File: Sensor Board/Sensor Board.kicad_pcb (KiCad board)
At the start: 2 copper layers, 44 parts, among them J1 Programming Header, J3 Micro_SD_Card, J4 CAN Bus Connector, U1 PIC18F26K83, U2 SPX3819M5-L-3-3, U3 MCP2562, U4 INA180, U5 OPA323IDCKR, Y1 12MHz Crystal

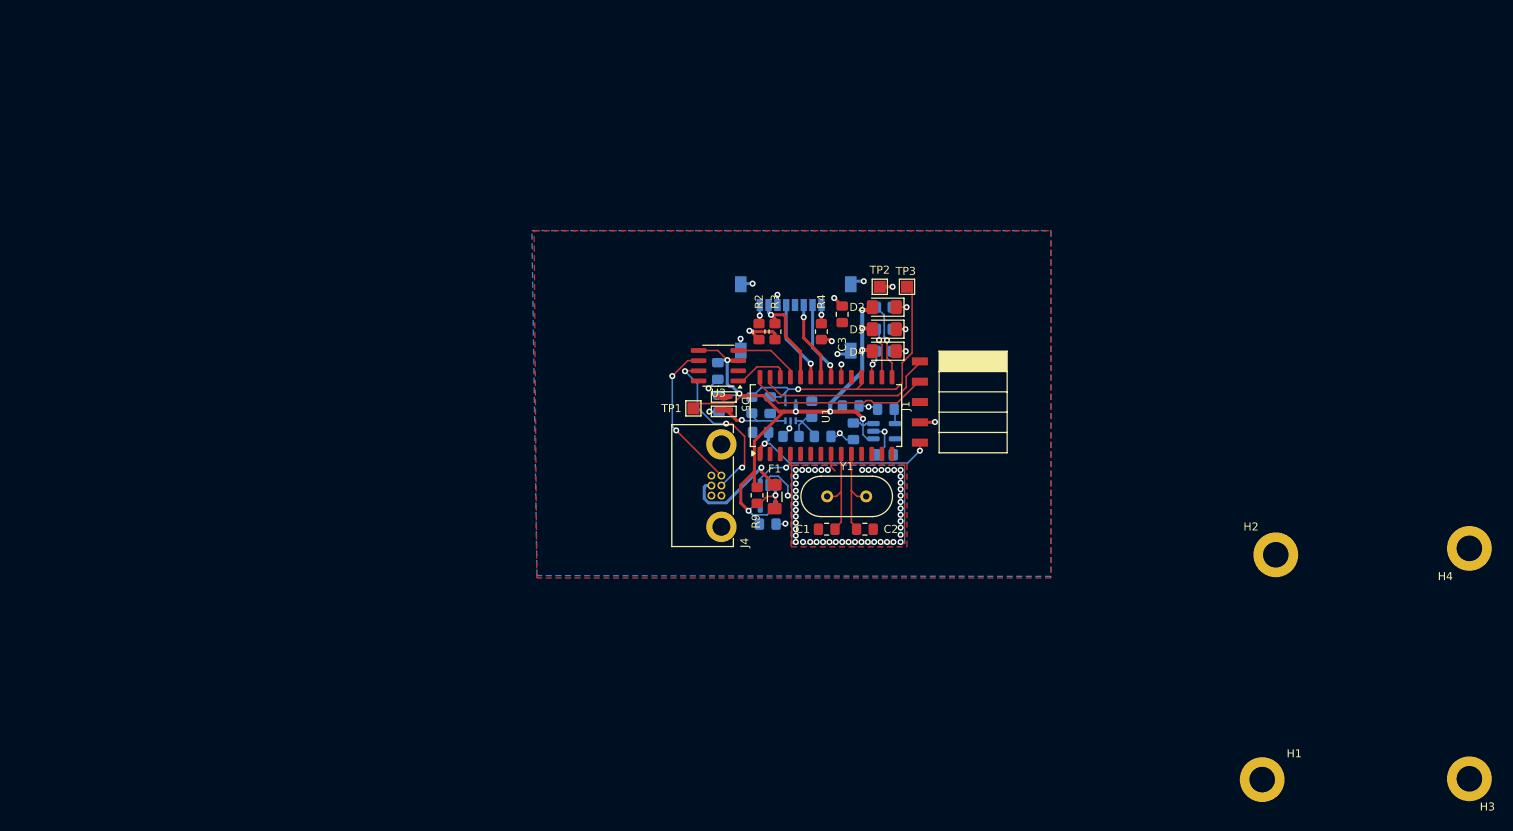
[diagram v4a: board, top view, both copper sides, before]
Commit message: fixed footprints not loading
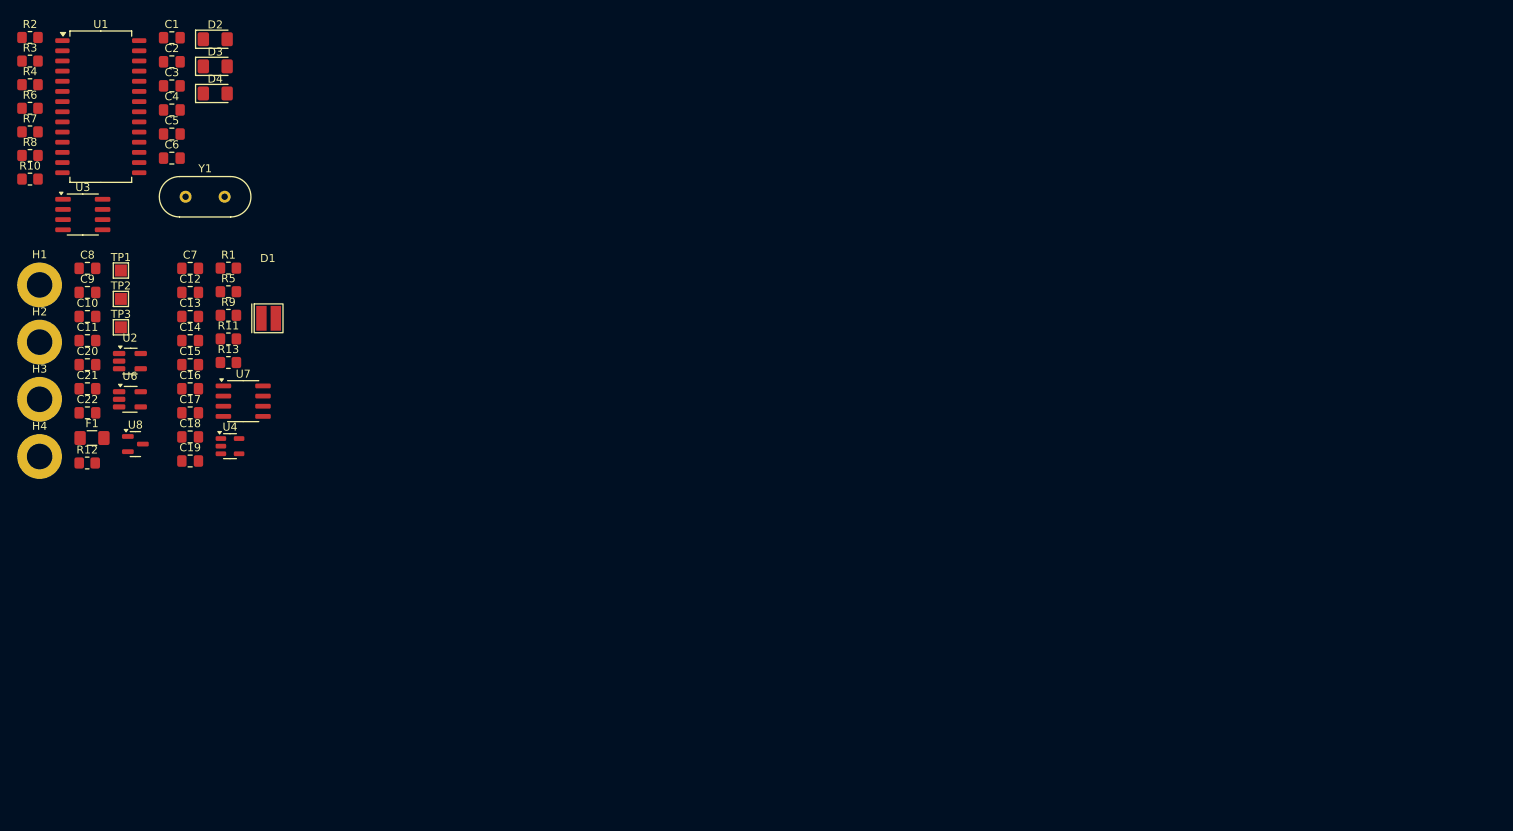
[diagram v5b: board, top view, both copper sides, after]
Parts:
- removed D5: Irr Sense, Canhw:P16612-011CA
- removed J1: Programming Header, Canhw:PinSocket_5x2.54_SMD_90deg_952-3198-1-ND
- removed J3: Micro_SD_Card, Canhw:microSD_Molex_WM6698CT-ND
- removed J4: CAN Bus Connector, Canhw:connector_Harwin_G125–MG10605M4P
- removed U5: OPA323IDCKR, Canhw:SC70-5_DCK_TEX
- added C14: 0.1uF, Capacitor_SMD:C_0805_2012Metric_Pad1.18x1.45mm_HandSolder, F.Cu at (70.7, 75.7)
- added C15: 0.1uF, Capacitor_SMD:C_0805_2012Metric_Pad1.18x1.45mm_HandSolder, F.Cu at (70.7, 78.7)
- added C16: 0.1uF, Capacitor_SMD:C_0805_2012Metric_Pad1.18x1.45mm_HandSolder, F.Cu at (70.7, 81.7)
- added C17: 0.1uF, Capacitor_SMD:C_0805_2012Metric_Pad1.18x1.45mm_HandSolder, F.Cu at (70.7, 84.8)
- added C18: 2.2uF, Capacitor_SMD:C_0805_2012Metric_Pad1.18x1.45mm_HandSolder, F.Cu at (70.7, 87.8)
- added C19: 2.2uF, Capacitor_SMD:C_0805_2012Metric_Pad1.18x1.45mm_HandSolder, F.Cu at (70.7, 90.8)
- added C20: 0.1uF, Capacitor_SMD:C_0805_2012Metric_Pad1.18x1.45mm_HandSolder, F.Cu at (57.9, 78.7)
- added C21: 1uF, Capacitor_SMD:C_0805_2012Metric_Pad1.18x1.45mm_HandSolder, F.Cu at (57.9, 81.7)
- added C22: 10uF, Capacitor_SMD:C_0805_2012Metric_Pad1.18x1.45mm_HandSolder, F.Cu at (57.9, 84.8)
- added C8: 0.1uF, Capacitor_SMD:C_0805_2012Metric_Pad1.18x1.45mm_HandSolder, F.Cu at (57.9, 66.7)
- added D1: P16612-011CA, SensorBoardFootprints:P16612-011CA, F.Cu at (80.4, 65.9)
- added R12: 200mR, Resistor_SMD:R_0805_2012Metric_Pad1.20x1.40mm_HandSolder, F.Cu at (57.8, 91.0)
- added R13: 10R, Resistor_SMD:R_0805_2012Metric_Pad1.20x1.40mm_HandSolder, F.Cu at (75.5, 78.5)
- added U6: SPX3819M5-L-3-3, Package_TO_SOT_SMD:SOT-23-5_HandSoldering, F.Cu at (63.2, 83.1)
- added U7: MCP1501-25xSN, Package_SO:SOIC-8_3.9x4.9mm_P1.27mm, F.Cu at (77.3, 83.3)
- added U8: MCP1754S-3302xCB, Package_TO_SOT_SMD:SOT-23, F.Cu at (63.8, 88.7)
- C10: value 10nF -> 0.1uF; moved to F.Cu
- C11: value 1uF -> 10nF; moved to F.Cu
- C12: value 2.5pF -> 1uF; moved to F.Cu
- C13: value 1uF -> 0.1uF; moved to F.Cu
- C4, C5, C6, C9, R10, R6, R7, R8: moved to F.Cu
- C7: value 0.1uF -> 4.7pF; moved to F.Cu
- R1: value 3MR -> 3.2M; moved to F.Cu
- R11: value 1kR -> 10R; moved to F.Cu
- R5: value 31kR -> 9.31k; moved to F.Cu
- R9: value 200mR -> 287R
- TP2: value 3.3v -> 3V3D
- TP3: value TestPoint -> 3V3A
- U2: value SPX3819M5-L-3-3 -> INA180; moved to F.Cu
- U4: value INA180 -> OPA323; footprint Package_TO_SOT_SMD:SOT-23-5_HandSoldering -> Package_TO_SOT_SMD:SOT-23-5; moved to F.Cu
- moved H3 184.9 mm to (51.9, 83.1)
- moved H4 179.1 mm to (51.9, 90.2)
- moved H1 164.9 mm to (51.9, 68.8)
- moved H2 156.8 mm to (51.9, 75.9)
- moved R6 109.6 mm to (50.7, 46.7), turned to 0 degrees
- moved R7 109.6 mm to (50.7, 49.6), turned to 0 degrees
- moved R10 108.9 mm to (50.7, 55.5), turned to 0 degrees
- moved C2 104.5 mm to (68.4, 40.9)
- moved R4 103.6 mm to (50.7, 43.7), turned to 0 degrees
- moved C1 102.3 mm to (68.4, 37.9), turned to 0 degrees
- moved C11 100.7 mm to (57.9, 75.7), turned to 0 degrees
- moved C10 100.5 mm to (57.9, 72.7), turned to 0 degrees
- moved R3 99.1 mm to (50.7, 40.8), turned to 0 degrees
- moved U1 98.5 mm to (59.5, 46.5), turned to 0 degrees
- moved TP3 98.4 mm to (62.0, 74.1)
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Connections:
- C10 pad 1: Net-(U2-BP) -> +5V
- C10 pad 2: GND -> AGND
- C11 pad 1: +3.3V -> Net-(U6-BP)
- C12 pad 1: /IRR_SENSE -> AGND
- C12 pad 2: Net-(D5-A) -> Net-(U4-+)
- C13 pad 1: GND -> AGND
- C13 pad 2: Net-(U5-IN+) -> Net-(U5-AVDD)
- C3 pad 2: +3.3V -> +3V3D
- C4 pad 1: +3.3V -> +3V3D
- C5 pad 2: +5V -> +3V3D
- C7 pad 1: +5V -> Net-(D1-A)
- C7 pad 2: GND -> Net-(U5-CH0)
- F1 pad 2: Net-(U4-IN+) -> Net-(U2-IN+)
- R1 pad 1: Net-(D5-A) -> Net-(D1-A)
- R1 pad 2: /IRR_SENSE -> Net-(U5-CH0)
- R11 pad 1: Net-(U5-IN+) -> +3V3A
- R11 pad 2: GND -> Net-(U5-AVDD)
- R2 pad 1: +3.3V -> +3V3D
- R3 pad 1: +3.3V -> +3V3D
- R4 pad 1: +3.3V -> +3V3D
- R5 pad 1: Net-(U5-IN+) -> +3V3A
- R5 pad 2: +3.3V -> Net-(U4-+)
- R6 pad 2: Net-(U1-RC4) -> Net-(U1-RA3)
- R7 pad 2: Net-(U1-RC5) -> Net-(U1-RA4)
- R8 pad 1: +3.3V -> +3V3D
- R9 pad 1: +5V -> AGND
- R9 pad 2: Net-(U4-IN+) -> Net-(U4-+)
- TP2 pad 1: +3.3V -> +3V3D
- TP3 pad 1: /IRR_SENSE -> +3V3A
- U1 pad 14: unconnected-(U1-RC3-Pad14) -> /SCLK
- U1 pad 15: Net-(U1-RC4) -> /MOSI
- U1 pad 16: Net-(U1-RC5) -> /MISO
- U1 pad 2: unconnected-(U1-RA0-Pad2) -> /MCLKIN
- U1 pad 20: +3.3V -> +3V3D
- U1 pad 3: unconnected-(U1-RA1-Pad3) -> /IRQ/MDAT
- U1 pad 5: unconnected-(U1-RA3-Pad5) -> Net-(U1-RA3)
- U1 pad 6: unconnected-(U1-RA4-Pad6) -> Net-(U1-RA4)
- U1 pad 7: unconnected-(U1-RA5-Pad7) -> /CS
- U2 pad 1: +5V -> /CURR_SENSE
- U2 pad 3: +5V -> Net-(U2-IN+)
- U2 pad 4: Net-(U2-BP) -> +5V
- U2 pad 5: +3.3V -> +3V3
- U3 pad 5: +5V -> +3V3D
- U4 pad 1: /CURR_SENSE -> Net-(U5-CH0)
- U4 pad 2: GND -> AGND
- U4 pad 3: Net-(U4-IN+) -> Net-(U4-+)
- U4 pad 4: +5V -> Net-(D1-A)
- U4 pad 5: +5V -> +3V3A
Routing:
- net +5V: track 88.6 -> 0.00 mm, vias 9 -> 0
- net /IRR_SENSE: track 38.1 -> 0.00 mm, vias 1 -> 0
- net GND: track 33.2 -> 0.00 mm, vias 63 -> 0
- net /~{MCLR}: track 25.7 -> 0.00 mm, vias 2 -> 0
- net /ICSPDAT: track 23.2 -> 0.00 mm
- net /ICSPCLK: track 22.9 -> 0.00 mm
- net /CANH: track 21.8 -> 0.00 mm, vias 3 -> 0
- net /CANL: track 19.1 -> 0.00 mm, vias 2 -> 0
- net Net-(J2-Pin_5): track 14.4 -> 0.00 mm, vias 1 -> 0
- net +3.3V: track 13.9 -> 0.00 mm, vias 6 -> 0
- net /PIC_MICRO_SD_SDI: track 12.9 -> 0.00 mm, vias 1 -> 0
- net /OSC2: track 11.8 -> 0.00 mm
- net /OSC1: track 11.7 -> 0.00 mm
- net Net-(D5-A): track 10.8 -> 0.00 mm, vias 1 -> 0
- net /PIC_MICRO_SD_SCK: track 10.3 -> 0.00 mm, vias 1 -> 0
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- removed copper zone on B.Cu, net +3.3V
- removed copper zone on B.Cu, net GND
- removed copper zone on F.Cu, net GND

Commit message: did layout
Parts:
- removed R2: 10kR, Resistor_SMD:R_0805_2012Metric_Pad1.20x1.40mm_HandSolder
- removed TP1: 5v, TestPoint:TestPoint_Pad_1.5x1.5mm
- removed TP2: 3V3D, TestPoint:TestPoint_Pad_1.5x1.5mm
- removed TP3: 3V3A, TestPoint:TestPoint_Pad_1.5x1.5mm
- added +3V3A: 3V3A, TestPoint:TestPoint_Pad_1.5x1.5mm, F.Cu at (221.7, 72.6)
- added +3V3D: 3V3D, TestPoint:TestPoint_Pad_1.5x1.5mm, F.Cu at (221.7, 77.7)
- added +5V: 5v, TestPoint:TestPoint_Pad_1.5x1.5mm, F.Cu at (221.7, 75.2)
- added C23: 0.1uF, Capacitor_SMD:C_0805_2012Metric_Pad1.18x1.45mm_HandSolder, F.Cu at (207.5, 59.7)
- added G***: LOGO, Team_Logo:Logo_SilkScreen_5mm, F.Cu at (191.0, 100.1)
- added J1: Programming Header, canhw:PinSocket_5x2.54_SMD_90deg_952-3198-1-ND, F.Cu at (190.5, 65.9)
- added J2: CAN Bus Connector, canhw:connector_Harwin_G125–MG10605M4P, F.Cu at (220.3, 87.1)
- added J3: Micro_SD_Card, canhw:microSD_Molex_WM6698CT-ND, B.Cu at (208.8, 100.8)
- added R14: 10kR, Resistor_SMD:R_0805_2012Metric_Pad1.20x1.40mm_HandSolder, B.Cu at (191.5, 100.6)
- added U5: MCP3561-E/ST, Package_SO:TSSOP-20_4.4x6.5mm_P0.65mm, F.Cu at (209.4, 71.4)
- C10, C11, C20, C21, C22, C3, C8, C9, F1, R12, R3, U2, U6, U8: moved to B.Cu
- moved R3 173.2 mm to (212.9, 101.6), turned to 180 degrees
- moved H2 169.9 mm to (220.0, 100.3)
- moved H1 168.4 mm to (220.0, 58.7)
- moved C11 161.4 mm to (217.9, 96.0)
- moved R4 160.0 mm to (201.2, 98.0), turned to 180 degrees
- moved U3 159.3 mm to (211.8, 98.6)
- moved C22 158.9 mm to (215.9, 68.6), turned to 180 degrees
- moved C20 158.6 mm to (215.9, 66.0), turned to 180 degrees
- moved F1 158.0 mm to (216.4, 85.6), turned to 90 degrees
- moved C9 155.5 mm to (211.9, 90.9), turned to -90 degrees
- moved R12 155.2 mm to (212.9, 85.1), turned to 90 degrees
- moved C21 155.1 mm to (212.3, 95.5), turned to 180 degrees
- moved C10 154.4 mm to (212.2, 72.1), turned to 90 degrees
- moved C5 154.2 mm to (213.4, 102.6)
- moved C3 153.8 mm to (212.3, 98.0)
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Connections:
- C8 pad 1: +3V3 -> +3V3D
- H1 pad 1: GND -> unconnected-(H1-Pad1)
- R10 pad 2: Net-(U1-RC6) -> Net-(U1-RA2)
- R13 pad 1: +3V3A -> +3V3D
- R3 pad 2: /PIC_MICRO_SD_SDI -> /MISO
- R4 pad 2: Net-(J3-DAT2) -> /MOSI
- U1 pad 11: unconnected-(U1-RC0-Pad11) -> /CANRX
- U1 pad 12: unconnected-(U1-RC1-Pad12) -> /CANTX
- U1 pad 15: /MOSI -> /MISO
- U1 pad 16: /MISO -> /MOSI
- U1 pad 17: Net-(U1-RC6) -> /CS_SD
- U1 pad 18: /IRR_SENSE -> unconnected-(U1-RC7-Pad18)
- U1 pad 21: /PIC_MICRO_SD_CS -> unconnected-(U1-RB0-Pad21)
- U1 pad 22: /PIC_MICRO_SD_SDO -> unconnected-(U1-RB1-Pad22)
- U1 pad 23: /PIC_MICRO_SD_SCK -> unconnected-(U1-RB2-Pad23)
- U1 pad 24: /PIC_MICRO_SD_SDI -> unconnected-(U1-RB3-Pad24)
- U1 pad 25: /CANRX -> unconnected-(U1-RB4-Pad25)
- U1 pad 26: /CANTX -> /CURR_SENSE
- U1 pad 4: /CURR_SENSE -> Net-(U1-RA2)
- U1 pad 7: /CS -> /CS_ADC
- U2 pad 5: +3V3 -> +3V3D
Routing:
- net +5V: track 0.00 -> 68.2 mm, vias 0 -> 6
- net /SCLK: track 0.00 -> 46.6 mm, vias 0 -> 1
- net /MISO: track 0.00 -> 39.2 mm, vias 0 -> 1
- net /~{MCLR}: track 0.00 -> 35.5 mm, vias 0 -> 3
- net /MOSI: track 0.00 -> 35.1 mm, vias 0 -> 1
- net +3V3D: track 0.00 -> 31.1 mm, vias 0 -> 20
- net /CANTX: track 0.00 -> 28.8 mm
- net /ICSPCLK: track 0.00 -> 27.9 mm, vias 0 -> 2
- net /ICSPDAT: track 0.00 -> 27.5 mm, vias 0 -> 2
- net /CANRX: track 0.00 -> 25.6 mm
- net /CS_ADC: track 0.00 -> 21.3 mm
- net GND: track 0.00 -> 21.0 mm, vias 0 -> 44
- net /MCLKIN: track 0.00 -> 20.9 mm
- net /CS_SD: track 0.00 -> 20.7 mm, vias 0 -> 1
- net /CANL: track 0.00 -> 20.6 mm
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- added copper zone on B.Cu, net +3V3A
- added copper zone on In2.Cu, net +3V3A
- added copper zone on B.Cu, net +3V3D
- added copper zone on In2.Cu, net +3V3D
- added copper zone on B.Cu, net +5V
- added copper zone on B.Cu, net AGND
- added copper zone on F.Cu, net AGND
- added copper zone on In1.Cu, net AGND
- added copper zone on B.Cu, net GND
- added copper zone on F.Cu, net GND
- added copper zone on In1.Cu, net GND
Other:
- board outline added: 41.7 x 49.5 mm
- copper layers 2 -> 4
- board text added: "1mW Infrared Detector DO NOT TOUCH LENSE KEEP OUT OF SUN 350mA @ 5V"
- board text added: "HOT!"
- board text added: "IR-Relevant Connor Stubbs Manav Toor 24-05-2025"
- board text added: "Waterloo Rocketry"
- board text added: "~{MCLR}"

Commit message: connected grounds
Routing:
- net (no net): track 0.00 -> 2.03 mm
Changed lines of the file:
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@@
 			(size 3.8 3.8)
 			(drill 2.25)
-			(layers "*.Cu" "*.Mask")
+			(layers "*.Cu" "*.Mask" "In3.Cu" "In4.Cu" "In5.Cu" "In6.Cu" "In7.Cu" "In8.Cu"
+				"In9.Cu" "In10.Cu" "In11.Cu" "In12.Cu" "In13.Cu" "In14.Cu" "In15.Cu"
+				"In16.Cu" "In17.Cu" "In18.Cu" "In19.Cu" "In20.Cu" "In21.Cu" "In22.Cu"
+				"In23.Cu" "In24.Cu" "In25.Cu" "In26.Cu" "In27.Cu" "In28.Cu" "In29.Cu"
+				"In30.Cu"
+			)
 			(remove_unused_layers no)
 		)
@@
 			(size 3.8 3.8)
 			(drill 2.25)
-			(layers "*.Cu" "*.Mask")
+			(layers "*.Cu" "*.Mask" "In3.Cu" "In4.Cu" "In5.Cu" "In6.Cu" "In7.Cu" "In8.Cu"
+				"In9.Cu" "In10.Cu" "In11.Cu" "In12.Cu" "In13.Cu" "In14.Cu" "In15.Cu"
+				"In16.Cu" "In17.Cu" "In18.Cu" "In19.Cu" "In20.Cu" "In21.Cu" "In22.Cu"
+				"In23.Cu" "In24.Cu" "In25.Cu" "In26.Cu" "In27.Cu" "In28.Cu" "In29.Cu"
+				"In30.Cu"
+			)
 			(remove_unused_layers no)
 		)
@@
 			(size 1 1)
 			(drill 0.6)
-			(layers "*.Cu" "*.Mask")
+			(layers "*.Cu" "*.Mask" "In3.Cu" "In4.Cu" "In5.Cu" "In6.Cu" "In7.Cu" "In8.Cu"
+				"In9.Cu" "In10.Cu" "In11.Cu" "In12.Cu" "In13.Cu" "In14.Cu" "In15.Cu"
+				"In16.Cu" "In17.Cu" "In18.Cu" "In19.Cu" "In20.Cu" "In21.Cu" "In22.Cu"
+				"In23.Cu" "In24.Cu" "In25.Cu" "In26.Cu" "In27.Cu" "In28.Cu" "In29.Cu"
+				"In30.Cu"
+			)
 			(remove_unused_layers no)
 			(net 44 "unconnected-(J2-Pin_1-Pad1)")
@@
 			(size 1 1)
 			(drill 0.6)
-			(layers "*.Cu" "*.Mask")
+			(layers "*.Cu" "*.Mask" "In3.Cu" "In4.Cu" "In5.Cu" "In6.Cu" "In7.Cu" "In8.Cu"
+				"In9.Cu" "In10.Cu" "In11.Cu" "In12.Cu" "In13.Cu" "In14.Cu" "In15.Cu"
+				"In16.Cu" "In17.Cu" "In18.Cu" "In19.Cu" "In20.Cu" "In21.Cu" "In22.Cu"
+				"In23.Cu" "In24.Cu" "In25.Cu" "In26.Cu" "In27.Cu" "In28.Cu" "In29.Cu"
+				"In30.Cu"
+			)
 			(remove_unused_layers no)
 			(net 30 "/CANH")
@@
 			(size 1 1)
 			(drill 0.6)
-			(layers "*.Cu" "*.Mask")
+			(layers "*.Cu" "*.Mask" "In3.Cu" "In4.Cu" "In5.Cu" "In6.Cu" "In7.Cu" "In8.Cu"
+				"In9.Cu" "In10.Cu" "In11.Cu" "In12.Cu" "In13.Cu" "In14.Cu" "In15.Cu"
+				"In16.Cu" "In17.Cu" "In18.Cu" "In19.Cu" "In20.Cu" "In21.Cu" "In22.Cu"
+				"In23.Cu" "In24.Cu" "In25.Cu" "In26.Cu" "In27.Cu" "In28.Cu" "In29.Cu"
+				"In30.Cu"
+			)
 			(remove_unused_layers no)
 			(net 29 "/CANL")
@@
 			(size 1 1)
 			(drill 0.6)
-			(layers "*.Cu" "*.Mask")
+			(layers "*.Cu" "*.Mask" "In3.Cu" "In4.Cu" "In5.Cu" "In6.Cu" "In7.Cu" "In8.Cu"
+				"In9.Cu" "In10.Cu" "In11.Cu" "In12.Cu" "In13.Cu" "In14.Cu" "In15.Cu"
+				"In16.Cu" "In17.Cu" "In18.Cu" "In19.Cu" "In20.Cu" "In21.Cu" "In22.Cu"
+				"In23.Cu" "In24.Cu" "In25.Cu" "In26.Cu" "In27.Cu" "In28.Cu" "In29.Cu"
+				"In30.Cu"
+			)
 			(remove_unused_layers no)
 			(net 54 "GND")
@@
 			(size 1 1)
 			(drill 0.6)
-			(layers "*.Cu" "*.Mask")
+			(layers "*.Cu" "*.Mask" "In3.Cu" "In4.Cu" "In5.Cu" "In6.Cu" "In7.Cu" "In8.Cu"
+				"In9.Cu" "In10.Cu" "In11.Cu" "In12.Cu" "In13.Cu" "In14.Cu" "In15.Cu"
+				"In16.Cu" "In17.Cu" "In18.Cu" "In19.Cu" "In20.Cu" "In21.Cu" "In22.Cu"
+				"In23.Cu" "In24.Cu" "In25.Cu" "In26.Cu" "In27.Cu" "In28.Cu" "In29.Cu"
+				"In30.Cu"
+			)
 			(remove_unused_layers no)
 			(net 34 "Net-(J2-Pin_5)")
@@
 			(size 1 1)
 			(drill 0.6)
-			(layers "*.Cu" "*.Mask")
+			(layers "*.Cu" "*.Mask" "In3.Cu" "In4.Cu" "In5.Cu" "In6.Cu" "In7.Cu" "In8.Cu"
+				"In9.Cu" "In10.Cu" "In11.Cu" "In12.Cu" "In13.Cu" "In14.Cu" "In15.Cu"
+				"In16.Cu" "In17.Cu" "In18.Cu" "In19.Cu" "In20.Cu" "In21.Cu" "In22.Cu"
+				"In23.Cu" "In24.Cu" "In25.Cu" "In26.Cu" "In27.Cu" "In28.Cu" "In29.Cu"
+				"In30.Cu"
+			)
 			(remove_unused_layers no)
 			(net 45 "unconnected-(J2-Pin_6-Pad6)")
@@
 			(size 5.6 5.6)
 			(drill 3.2)
-			(layers "*.Cu" "*.Mask")
+			(layers "*.Cu" "*.Mask" "In3.Cu" "In4.Cu" "In5.Cu" "In6.Cu" "In7.Cu" "In8.Cu"
+				"In9.Cu" "In10.Cu" "In11.Cu" "In12.Cu" "In13.Cu" "In14.Cu" "In15.Cu"
+				"In16.Cu" "In17.Cu" "In18.Cu" "In19.Cu" "In20.Cu" "In21.Cu" "In22.Cu"
+				"In23.Cu" "In24.Cu" "In25.Cu" "In26.Cu" "In27.Cu" "In28.Cu" "In29.Cu"
+				"In30.Cu"
+			)
 			(remove_unused_layers no)
 			(net 55 "unconnected-(H1-Pad1)")
@@
 			(size 5.6 5.6)
 			(drill 3.2)
-			(layers "*.Cu" "*.Mask")
+			(layers "*.Cu" "*.Mask" "In3.Cu" "In4.Cu" "In5.Cu" "In6.Cu" "In7.Cu" "In8.Cu"
+				"In9.Cu" "In10.Cu" "In11.Cu" "In12.Cu" "In13.Cu" "In14.Cu" "In15.Cu"
+				"In16.Cu" "In17.Cu" "In18.Cu" "In19.Cu" "In20.Cu" "In21.Cu" "In22.Cu"
+				"In23.Cu" "In24.Cu" "In25.Cu" "In26.Cu" "In27.Cu" "In28.Cu" "In29.Cu"
+				"In30.Cu"
+			)
 			(remove_unused_layers no)
 			(net 54 "GND")
@@
 			(size 5.6 5.6)
 			(drill 3.2)
-			(layers "*.Cu" "*.Mask")
+			(layers "*.Cu" "*.Mask" "In3.Cu" "In4.Cu" "In5.Cu" "In6.Cu" "In7.Cu" "In8.Cu"
+				"In9.Cu" "In10.Cu" "In11.Cu" "In12.Cu" "In13.Cu" "In14.Cu" "In15.Cu"
+				"In16.Cu" "In17.Cu" "In18.Cu" "In19.Cu" "In20.Cu" "In21.Cu" "In22.Cu"
+				"In23.Cu" "In24.Cu" "In25.Cu" "In26.Cu" "In27.Cu" "In28.Cu" "In29.Cu"
+				"In30.Cu"
+			)
 			(remove_unused_layers no)
 			(net 54 "GND")
@@
 			(size 5.6 5.6)
 			(drill 3.2)
-			(layers "*.Cu" "*.Mask")
+			(layers "*.Cu" "*.Mask" "In3.Cu" "In4.Cu" "In5.Cu" "In6.Cu" "In7.Cu" "In8.Cu"
+				"In9.Cu" "In10.Cu" "In11.Cu" "In12.Cu" "In13.Cu" "In14.Cu" "In15.Cu"
+				"In16.Cu" "In17.Cu" "In18.Cu" "In19.Cu" "In20.Cu" "In21.Cu" "In22.Cu"
+				"In23.Cu" "In24.Cu" "In25.Cu" "In26.Cu" "In27.Cu" "In28.Cu" "In29.Cu"
+				"In30.Cu"
+			)
 			(remove_unused_layers no)
 			(net 54 "GND")
@@
 			(size 1.5 1.5)
 			(drill 0.8)
-			(layers "*.Cu" "*.Mask")
+			(layers "*.Cu" "*.Mask" "In3.Cu" "In4.Cu" "In5.Cu" "In6.Cu" "In7.Cu" "In8.Cu"
+				"In9.Cu" "In10.Cu" "In11.Cu" "In12.Cu" "In13.Cu" "In14.Cu" "In15.Cu"
+				"In16.Cu" "In17.Cu" "In18.Cu" "In19.Cu" "In20.Cu" "In21.Cu" "In22.Cu"
+				"In23.Cu" "In24.Cu" "In25.Cu" "In26.Cu" "In27.Cu" "In28.Cu" "In29.Cu"
+				"In30.Cu"
+			)
 			(remove_unused_layers no)
 			(net 1 "/OSC1")
@@
 			(size 1.5 1.5)
 			(drill 0.8)
-			(layers "*.Cu" "*.Mask")
+			(layers "*.Cu" "*.Mask" "In3.Cu" "In4.Cu" "In5.Cu" "In6.Cu" "In7.Cu" "In8.Cu"
+				"In9.Cu" "In10.Cu" "In11.Cu" "In12.Cu" "In13.Cu" "In14.Cu" "In15.Cu"
+				"In16.Cu" "In17.Cu" "In18.Cu" "In19.Cu" "In20.Cu" "In21.Cu" "In22.Cu"
+				"In23.Cu" "In24.Cu" "In25.Cu" "In26.Cu" "In27.Cu" "In28.Cu" "In29.Cu"
+				"In30.Cu"
+			)
 			(remove_unused_layers no)
 			(net 2 "/OSC2")
@@
 	)
 	(segment
+		(start 192.024 58.42)
+		(end 189.992 58.42)
+		(width 1.27)
+		(layer "In1.Cu")
+		(net 0)
+	)
+	(segment
